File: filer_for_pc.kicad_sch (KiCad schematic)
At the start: 50 parts

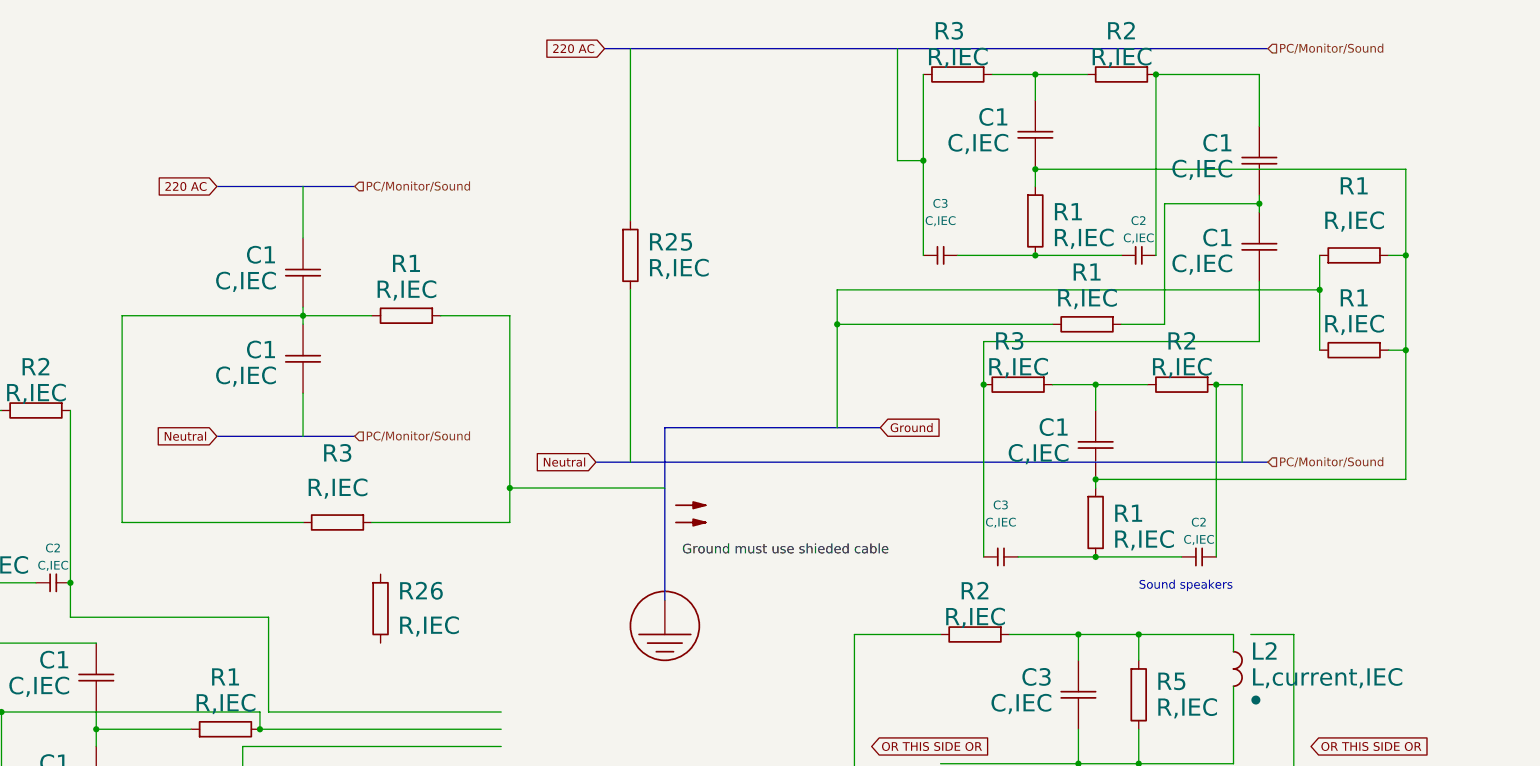
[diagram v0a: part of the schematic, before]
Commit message: Upgrader to Grounding device
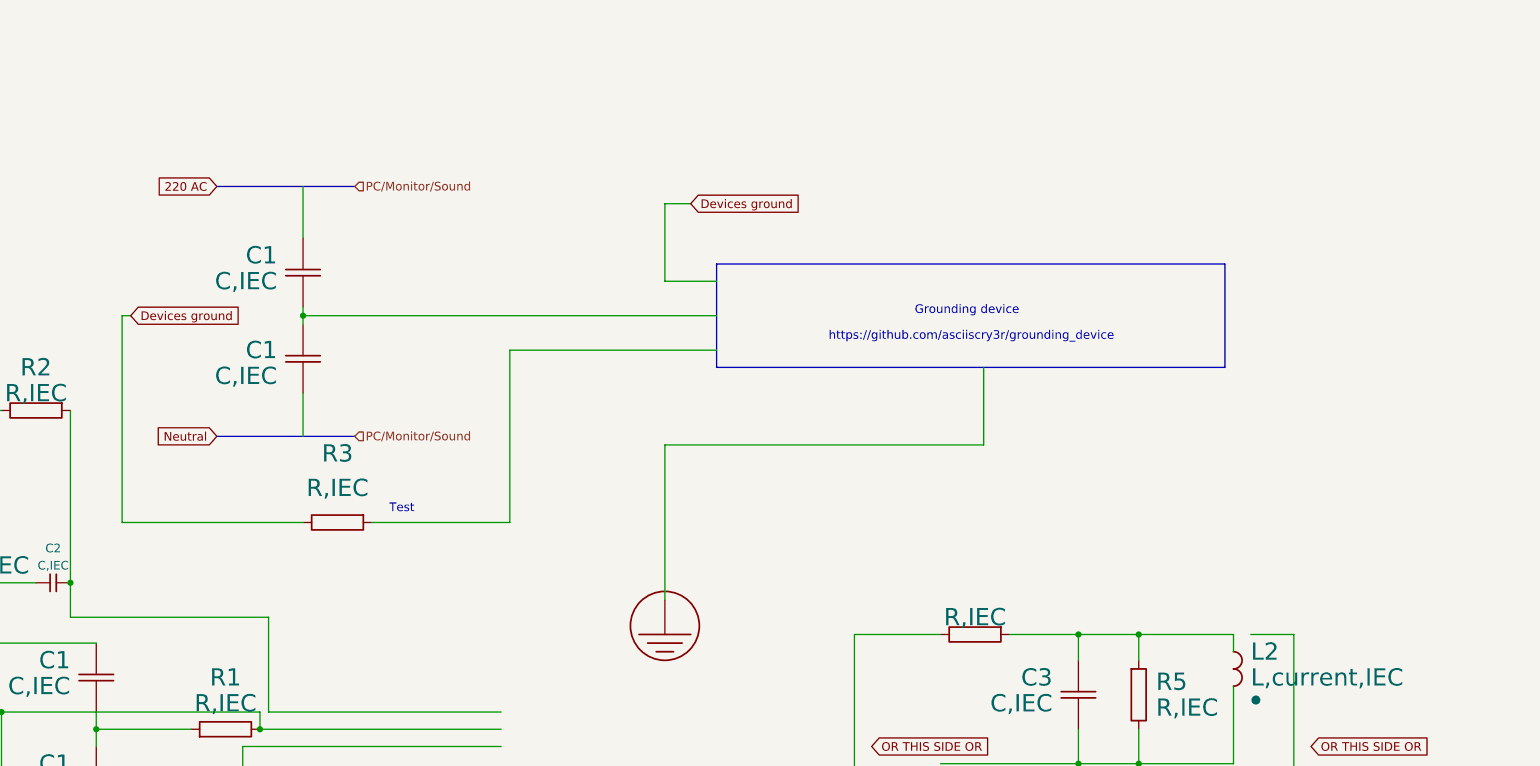
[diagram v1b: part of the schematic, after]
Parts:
- removed C1 (x4): C,IEC, symbol PCM_Generic:C,IEC
- removed C2 (x2), C3 (x2): C,IEC, symbol PCM_Generic-50:C,IEC
- removed R1 (x6), R2 (x2), R25, R26, R3 (x2): R,IEC, symbol PCM_Generic:R,IEC
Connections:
- net at C1.1 (+), C1.2 (-): no longer R3.2 (-)
- new net Devices ground: R3.2 (-)
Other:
- note added: "Grounding device"
- note added: "Test"
- note added: "https://github.com/asciiscry3r/grounding_device"

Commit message: Upgrade
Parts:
- added C1 (x2): C,IEC, symbol PCM_Generic:C,IEC
- added L3, L4, L5, L6: L, symbol PCM_Elektuur:L
- added R1: R,IEC, symbol PCM_Generic:R,IEC
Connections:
- net 220 AC: now also L5.1 (+), L5.2 (-), L6.1 (+), L6.2 (-)
- net at C1.1 (+), C1.2 (-), R1.1 (+): now also R1.2 (-), R1.2 (-), R19.1 (+), C1.1 (+), C1.2 (-), R1.1 (+), R1.2 (-)
- net at R9.2 (-): no longer R6.2 (-)
- net at C2.1 (+), R2.1 (+): now also C1.1 (+)
- net at C2.1 (+), R2.1 (+): now also C1.2 (-)
- net at R6.1 (+): no longer R2.2 (-)
- new net 12-9 AC: L3.1 (+), L3.2 (-), L4.1 (+), L4.2 (-)
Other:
- moved on the sheet: C1, C2, C3, R1, R19, R2, R3

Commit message: Upgrade
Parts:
- added C1 (x2): C,IEC, symbol PCM_Generic:C,IEC
- added R4: R,IEC, symbol PCM_Generic:R,IEC
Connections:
- net 220 AC: no longer L5.2 (-), L6.1 (+)
- net Devices ground: no longer R3.2 (-)
- net at C1.1 (+), C1.2 (-): now also R3.2 (-)
- new net: C1.1 (+), C1.2 (-), R4.2 (-)
- new net neutral: L5.2 (-), L6.1 (+)
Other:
- note added: "04.09.2023"
- note added: "5 filters with HF resistors and 6 without"
- note removed: "Test"
- moved on the sheet: R3

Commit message: Upgrade
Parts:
- added R1 (x2), R8: R,IEC, symbol PCM_Generic:R,IEC
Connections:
- net Neutral: now also C1.2 (-)
- net Line: now reaches C1.1 (+)
- net at C1.1 (+), C1.2 (-), R4.2 (-): now also R8.2 (-)
- net at R4.1 (+): now also R8.1 (+)
- new net: C1.1 (+), C1.2 (-), R1.1 (+), R1.1 (+)
- new net: R1.2 (-), R1.2 (-), R1.2 (-), R1.2 (-)
- new net: C1.1 (+), C1.2 (-), R1.1 (+), R1.1 (+), R1.2 (-), R19.1 (+)
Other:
- note added: "5 filters with HF resistors and more then 6 without"
- note added: "Optional"
- note added: "Sound Power Source"
- note removed: "5 filters with HF resistors and 6 without"
- moved on the sheet: C1, R1, R4

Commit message: Upgrade
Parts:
- added C10, C11, C20, C9: 100uF, symbol PCM_Generic:C,IEC
- added C22, C23: C,IEC, symbol PCM_Generic:C,IEC
- added J1: Ethernet In, 4ms_Connector:Pins_1x08_2.54mm_TH, symbol PCM_4ms_Connector:Conn_01x08
- added J2: Ethernet Out, 4ms_Connector:Pins_1x08_2.54mm_TH, symbol PCM_4ms_Connector:Conn_01x08
- added R13, R14, R15, R24: 10 Om, symbol PCM_Generic:R,IEC
- added R26, R27: R,IEC, symbol PCM_Generic:R,IEC
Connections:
- net at C7.1 (+), L1.1 (+), R11.1 (+)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: now also C23.1 (+)
- net at C7.2 (-), L1.2 (-), R11.2 (-): now also R27.2 (-)
- net at C3.1 (+), L2.1 (+), R2.1 (+)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: now also C22.1 (+)
- net at C3.2 (-), L2.2 (-), R5.2 (-): now also R26.2 (-)
- net at C1.1 (+), C2.1 (+), R2.1 (+): now also C1.1 (+)
- net at C1.2 (-), C2.1 (+), R2.1 (+): now also C1.2 (-)
- new net: C9.1 (+), J1.1 (Pin_1), J2.1 (Pin_1)
- new net: C9.2 (-), R13.1 (+)
- new net: C10.1 (+), J1.5 (Pin_5), J2.5 (Pin_5)
- new net: C10.2 (-), R15.1 (+)
- new net: C22.2 (-), R26.1 (+)
- new net: R13.2 (-), R14.2 (-), R15.2 (-), R24.2 (-)
- new net: J1.2 (Pin_2), J2.2 (Pin_2)
- new net: C11.1 (+), J1.3 (Pin_3), J2.3 (Pin_3)
- new net: J1.4 (Pin_4), J2.4 (Pin_4)
- new net: J1.6 (Pin_6), J2.6 (Pin_6)
- new net: C20.1 (+), J1.7 (Pin_7), J2.7 (Pin_7)
- new net: J1.8 (Pin_8), J2.8 (Pin_8)
- new net: C11.2 (-), R14.1 (+)
- new net: C20.2 (-), R24.1 (+)
- new net: C23.2 (-), R27.1 (+)
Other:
- note added: "Upgrade 2023.10.23"
- note removed: "Optional"
- moved on the sheet: C1, C2, C3, C7, L1, L2, L3, L4, L5, L6, R1, R11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

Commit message: Upgrade
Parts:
- removed R1 (x2): R,IEC, symbol PCM_Generic:R,IEC
- added C21, C24, C25, C26: 1uF, symbol PCM_Generic:C,IEC
- added C27, C28: C, 22 pF, symbol PCM_Generic:C,IEC
- added R10, R20, R25: 10 Om, symbol PCM_Generic:R,IEC
- added R29, R30: R, 90 Om, symbol PCM_Generic:R,IEC
- C10, C11, C20, C9: value 100uF -> 1uF
- R4: value R,IEC -> 10 Om
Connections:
- net at C7.1 (+), L1.1 (+), R11.1 (+)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: now also C28.2 (-); no longer C23.1 (+)
- net at C7.2 (-), L1.2 (-), R11.2 (-)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: now also R30.2 (-)
- net at C3.1 (+), L2.1 (+), R2.1 (+)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: now also C27.2 (-); no longer C22.1 (+)
- net at C3.2 (-), L2.2 (-), R26.2 (-)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: now also R29.2 (-)
- net at R9.2 (-): now also C23.2 (-), R27.1 (+)
- net at C22.2 (-), R26.1 (+): now also R2.2 (-)
- net at C1.1 (+), C1.2 (-), R8.2 (-): no longer R4.2 (-)
- net at R13.2 (-), R14.2 (-), R15.2 (-)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: now also R4.2 (-), R10.2 (-), R20.2 (-), R25.2 (-)
- net at J1.2 (Pin_2), J2.2 (Pin_2): now also C26.1 (+)
- net at J1.4 (Pin_4), J2.4 (Pin_4): now also C24.1 (+)
- net at J1.6 (Pin_6), J2.6 (Pin_6): now also C25.1 (+)
- net at C20.1 (+), J1.7 (Pin_7), J2.7 (Pin_7): now also J1.8 (Pin_8), J2.8 (Pin_8), C21.1 (+)
- net at R4.1 (+): now also C21.2 (-); no longer R8.1 (+)
- new net: C25.2 (-), R20.1 (+)
- new net: C28.1 (+), R30.1 (+)
- new net: C24.2 (-), R10.1 (+)
- new net: C26.2 (-), R25.1 (+)
- new net: C27.1 (+), R29.1 (+)
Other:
- moved on the sheet: C20, C22, C23, R26, R6, R9

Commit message: Upgrade
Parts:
- removed C10, C11, C20, C21, C24, C25, C9: 1uF, symbol PCM_Generic:C,IEC
- removed L3, L4, L5, L6: L, symbol PCM_Elektuur:L
- added C10, C11, C20, C21, C24, C25, C29, C9: ~50uF, symbol PCM_Elektuur:C-polar
- added C30, C41, C43: C, 100 nF, symbol PCM_Generic:C,IEC
- added C31, C32, C34, C39, C47, C48: C, 22 pF, symbol PCM_Generic:C,IEC
- added C33, C40: C, 10 nF, symbol PCM_Generic:C,IEC
- added C35, C38, C42, C44: C,1uF, symbol PCM_Generic:C,IEC
- added C36, C37, C45, C46: C,680pF, symbol PCM_Generic:C,IEC
- added L3: L,Sound speaker L, symbol PCM_Generic:L,current,IEC
- added L4: L, Sound speaker R, symbol PCM_Generic:L,current,IEC
- added L5: L, Sound speaker L, symbol PCM_Generic:L,current,IEC
- added L6: L,Sound speaker R, symbol PCM_Generic:L,current,IEC
- added R31, R32, R33, R34, R36, R43, R45, R46, R53: R, 10 Om, symbol PCM_Generic:R,IEC
- added R35, R52: R, 90 Om, symbol PCM_Generic:R,IEC
- added R37, R42, R44: R,10KoM, symbol PCM_Generic:R,IEC
- added R38: R, 10 MOM, symbol PCM_Generic:R,IEC
- added R39, R50: R,10Om, symbol PCM_Generic:R,IEC
- added R40, R48: R,10 Om, symbol PCM_Generic:R,IEC
- added R41, R49: R,10MoM, symbol PCM_Generic:R,IEC
- added R47: R,10 KoM, symbol PCM_Generic:R,IEC
- added R51: R,10 MOM, symbol PCM_Generic:R,IEC
- C26: value 1uF -> C, 100 nF
- L1: value L,current,IEC -> L, Sound speaker
- L2: value L,current,IEC -> L,Sound speaker
- R7: value R,IEC -> R, 10 Om
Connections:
- net at C28.2 (-), C7.1 (+), L1.1 (+)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: now also C32.1 (+)
- net GND: now reaches C7.2 (-), L1.2 (-), R11.2 (-), R27.2 (-), R30.2 (-)
- net GND: now also C26.2 (-), C3.2 (-), L2.2 (-), R26.2 (-), R29.2 (-), R5.2 (-), R7.2 (-), C30.2 (-), R33.2 (-)
- net at C27.2 (-), C3.1 (+), L2.1 (+)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: now also C31.2 (-)
- net at J1.6 (Pin_6), J2.6 (Pin_6): now also C10.2 (-)
- net at R20.1 (+): now also C10.1 (+)
- net at J1.1 (Pin_1), J2.1 (Pin_1): now also C20.1 (+)
- net at R13.1 (+): now also C20.2 (-)
- net at R7.1 (+): now also C31.1 (+)
- net at J1.5 (Pin_5), J2.5 (Pin_5): now also C21.1 (+)
- net at R15.1 (+): now also C21.2 (-)
- net at C22.1 (+): now also R6.1 (+), R32.1 (+)
- net at R10.1 (+): now also C29.2 (-)
- net at C1.1 (+), C1.2 (-): now also R8.1 (+); no longer R8.2 (-)
- net at R25.1 (+): now also C25.1 (+); no longer C26.2 (-)
- net at J1.2 (Pin_2), J2.2 (Pin_2): now also C25.2 (-); no longer C26.1 (+)
- net at J1.4 (Pin_4), J2.4 (Pin_4): now also C24.2 (-)
- net at R4.1 (+): now also C11.1 (+)
- net at J1.3 (Pin_3), J2.3 (Pin_3): now also C9.1 (+)
- net at J1.7 (Pin_7), J2.7 (Pin_7): now also C29.1 (+); no longer J1.8 (Pin_8), J2.8 (Pin_8)
- net at R14.1 (+): now also C9.2 (-)
- net at R6.2 (-): now also C23.1 (+), R31.1 (+)
- net at R24.1 (+): now also C24.1 (+)
- new net: C36.1 (+), L4.1 (+), R38.1 (+), R39.1 (+)
- new net: C38.2 (-), R39.2 (-), R42.1 (+)
- new net: C39.2 (-), R43.1 (+)
- new net: C35.2 (-), R37.1 (+), R40.2 (-)
- new net: C34.2 (-), C37.2 (-), C39.1 (+), C44.1 (+), L3.2 (-), R34.2 (-), R36.2 (-), R37.2 (-), R41.2 (-)
- new net: C45.1 (+), L5.1 (+), R48.1 (+), R49.1 (+)
- new net: C32.2 (-), R33.1 (+)
- new net: C37.1 (+), L3.1 (+), R40.1 (+), R41.1 (+)
- new net: C44.2 (-), R47.1 (+), R48.2 (-)
- new net: C11.2 (-), J1.8 (Pin_8), J2.8 (Pin_8)
- new net: C47.1 (+), R52.1 (+)
- new net: C38.1 (+), C46.2 (-), C47.2 (-), C48.1 (+), L6.2 (-), R44.2 (-), R45.2 (-), R46.2 (-), R51.2 (-)
- new net: C46.1 (+), L6.1 (+), R50.1 (+), R51.1 (+)
- new net: C40.1 (+), R46.1 (+)
- new net: C41.1 (+), R45.1 (+)
- new net: C42.2 (-), R44.1 (+), R50.2 (-)
- new net: C34.1 (+), R35.1 (+)
- new net: C26.1 (+), R31.2 (-)
- new net: C33.1 (+), R36.1 (+)
- new net: C43.1 (+), R34.1 (+)
- new net: C30.1 (+), R32.2 (-)
- new net: C48.2 (-), R53.1 (+)
- new net GNDA: C33.2 (-), C35.1 (+), C36.2 (-), C40.2 (-), C41.2 (-), C42.1 (+), C43.2 (-), C45.2 (-), L4.2 (-), L5.2 (-), R35.2 (-), R38.2 (-), R42.2 (-), R43.2 (-), R47.2 (-), R49.2 (-), R52.2 (-), R53.2 (-)
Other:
- note added: "1969 PRO JLH Class"
- note removed: "Sound Power Source"
- note removed: "Sound speakers"
- moved on the sheet: C1, C22, C23, C27, C28, C3, C7, L1, L2, R11, R24, R25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

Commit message: Upgrade
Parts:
- removed C1 (x8): C,IEC, symbol PCM_Generic:C,IEC
- removed C10, C11, C24, C25: ~50uF, symbol PCM_Elektuur:C-polar
- removed C2 (x2), C3 (x2): C,IEC, symbol PCM_Generic-50:C,IEC
- removed C33, C40: C, 10 nF, symbol PCM_Generic:C,IEC
- removed C34, C39, C47, C48: C, 22 pF, symbol PCM_Generic:C,IEC
- removed C35, C38, C42, C44: C,1uF, symbol PCM_Generic:C,IEC
- removed C36, C37, C45, C46: C,680pF, symbol PCM_Generic:C,IEC
- removed C41, C43: C, 100 nF, symbol PCM_Generic:C,IEC
- removed L3: L,Sound speaker L, symbol PCM_Generic:L,current,IEC
- removed L4: L, Sound speaker R, symbol PCM_Generic:L,current,IEC
- removed L5: L, Sound speaker L, symbol PCM_Generic:L,current,IEC
- removed L6: L,Sound speaker R, symbol PCM_Generic:L,current,IEC
- removed R1 (x5), R11, R19, R2 (x2), R3 (x3), R5: R,IEC, symbol PCM_Generic:R,IEC
- removed R20, R24, R25, R4: 10 Om, symbol PCM_Generic:R,IEC
- removed R34, R36, R43, R45, R46, R53: R, 10 Om, symbol PCM_Generic:R,IEC
- removed R35, R52: R, 90 Om, symbol PCM_Generic:R,IEC
- removed R37, R42, R44: R,10KoM, symbol PCM_Generic:R,IEC
- removed R38: R, 10 MOM, symbol PCM_Generic:R,IEC
- removed R39, R50: R,10Om, symbol PCM_Generic:R,IEC
- removed R40, R48: R,10 Om, symbol PCM_Generic:R,IEC
- removed R41, R49: R,10MoM, symbol PCM_Generic:R,IEC
- removed R47: R,10 KoM, symbol PCM_Generic:R,IEC
- removed R51: R,10 MOM, symbol PCM_Generic:R,IEC
- added AE1, AE2: Antenna, symbol Device:Antenna
- added C1, C2, C4, C5: C, symbol Device:C
- added D1, D10, D11, D12, D13, D14, D15, D16, D2, D3, D4, D5, D6, D7, D8, D9: D, symbol Device:D
- added L3, L4, L5, L6: L, symbol Device:L
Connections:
- new net: C5.2, D13.2 (A), D15.1 (K)
- new net: D15.2 (A), D16.1 (K)
- new net: C1.2, D5.1 (K), D6.2 (A)
- new net: C2.2, D5.2 (A), D7.1 (K)
- new net: D3.1 (K), D4.2 (A), L4.1
- new net: D2.1 (K), D3.2 (A), L3.1
- new net: D11.2 (A), D12.1 (K)
- new net: D10.1 (K), D12.2 (A), L6.1
- new net: D10.2 (A), D9.1 (K), L5.1
- new net: AE2.1 (A), D11.1 (K), D9.2 (A)
- new net: AE1.1 (A), D1.1 (K), D2.2 (A)
- new net: D1.2 (A), D4.1 (K)
- new net: C1.1, L3.2
- new net: C4.1, L5.2
- new net: D7.2 (A), D8.1 (K)
- new net: D14.1 (K), D16.2 (A), D6.1 (K), D8.2 (A)
- new net: C2.1, L4.2
- new net: C5.1, L6.2
- new net: C4.2, D13.1 (K), D14.2 (A)
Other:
- note added: "1 M"
- note added: "20 M"
- note added: "3 M"
- note added: "40 M"
- note added: "For this, pirates turn off the Internet over twisted pair cables and break mobile phones, as well as for firewalls on the computer and on the router, the adaptive ASA firewall seems to have been completely killed"
- note removed: "1969 PRO JLH Class"
